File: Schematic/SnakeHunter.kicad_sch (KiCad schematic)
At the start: 17 parts, among them J1 Conn_01x04_Pin, J2 Conn_01x04_Pin, SW1 SW_Nidec_CAS-120A1, SW3 SW_DIP_x02, U2 CR2013-MI2120, U3 TSDP341xx, U4 NRF24L01_Breakout, U5 CRE1S0305S3C

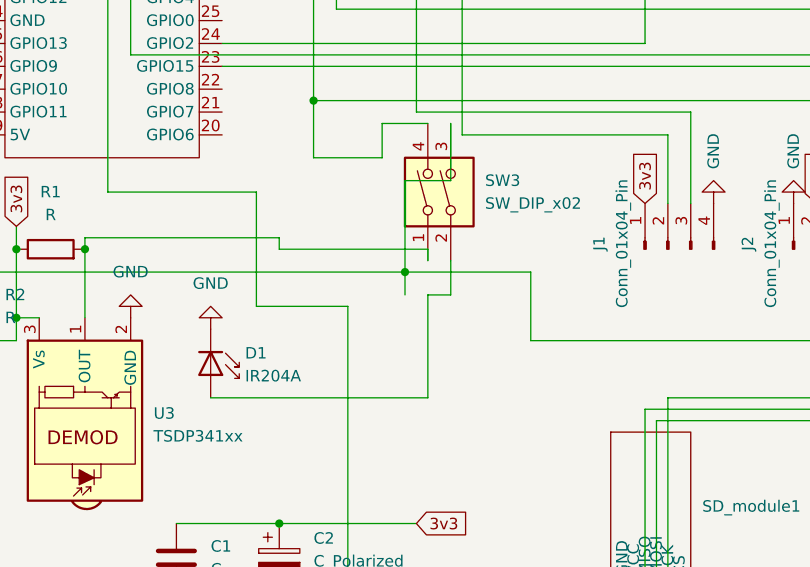
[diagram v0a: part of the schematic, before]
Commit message: Remove unused PCB because of using handwiring.
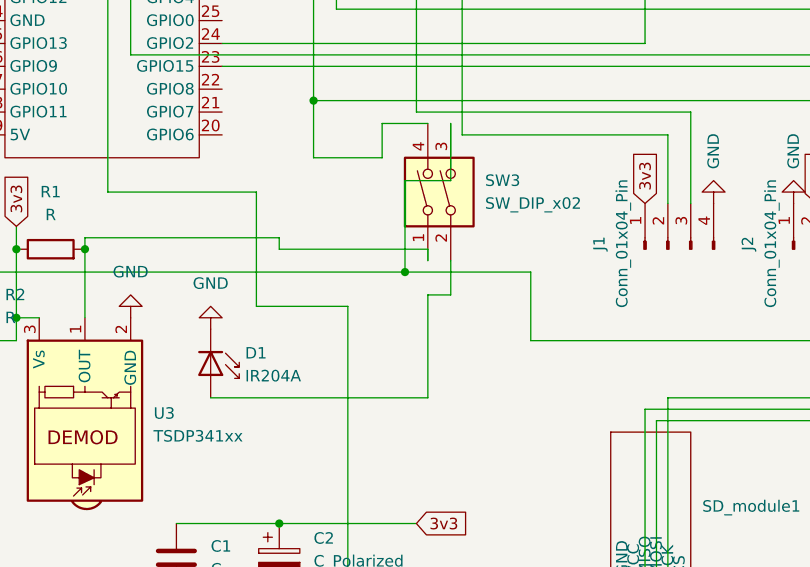
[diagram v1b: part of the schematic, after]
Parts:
- Charging_module1: footprint (none) -> my:charging chip
- J1: footprint (none) -> my:GPS
- J2: footprint (none) -> my:RFID
- R1, R2: footprint Resistor_THT:R_Array_SIP4 -> Resistor_THT:R_Axial_DIN0204_L3.6mm_D1.6mm_P5.08mm_Horizontal
- SD_module1: footprint (none) -> my:SD module
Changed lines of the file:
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@@
-	(wire
-		(pts
-			(xy 63.5 81.28) (xy 63.5 78.74)
-		)
-		(stroke
-			(width 0)
-			(type default)
-		)
-	)
 	(wire
 		(pts
@@
 			)
 		)
-		(property "Footprint" ""
+		(property "Footprint" "my:SD module"
 			(at 96.52 102.87 0)
 			(effects
@@
 			)
 		)
-		(property "Footprint" ""
+		(property "Footprint" "my:charging chip"
 			(at 156.21 121.92 0)
 			(effects
@@
 			)
 		)
-		(property "Footprint" ""
+		(property "Footprint" "my:RFID"
 			(at 109.22 76.2 0)
 			(effects
@@
 			)
 		)
-		(property "Footprint" "Resistor_THT:R_Array_SIP4"
+		(property "Footprint" "Resistor_THT:R_Axial_DIN0204_L3.6mm_D1.6mm_P5.08mm_Horizontal"
 			(at 18.288 82.55 90)
 			(effects
@@
 			)
 		)
-		(property "Footprint" ""
+		(property "Footprint" "my:GPS"
 			(at 92.71 76.2 0)
 			(effects
@@
 			)
 		)
-		(property "Footprint" "Resistor_THT:R_Array_SIP4"
+		(property "Footprint" "Resistor_THT:R_Axial_DIN0204_L3.6mm_D1.6mm_P5.08mm_Horizontal"
 			(at 24.13 77.978 90)
 			(effects

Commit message: Schematic moreee cleannn
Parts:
- J1: value Conn_01x04_Pin -> GPS module
- J2: value Conn_01x04_Pin -> RFID module
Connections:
- net GND: now also SW1.2 (B), U1.14 (GND), U2.2 (GND)
- net T-DO: now reaches U1.4 (GPI39), U2.15 (T-DO)
- net T-IRQ: now reaches U1.3 (GPI36), U2.16 (T-IRQ)
- net T-DIN: now reaches U1.7 (GPIO32), U2.17 (T-DIN)
- net T-CS: now reaches U1.8 (GPIO33), U2.18 (T-CS)
- net T-CLK: now reaches U1.9 (GPIO25), U2.19 (T-CLK)
- net CS: now reaches U1.23 (GPIO15), U2.3 (~{CS})
- net RESET: now reaches U1.2 (EN), U2.4 (RESET)
- net D/C: now reaches U1.24 (GPIO2), U2.5 (D/~{C})
- net MOSI: now reaches U1.15 (GPIO13), U2.6 (MOSI)
- net SCK: now reaches U1.12 (GPIO14), U2.7 (SCK)
- net LED: now reaches U1.33 (GPIO21), U2.8 (LED)
- net MISO: now reaches U1.13 (GPIO12), U2.9 (MISO)
- net CSN: now reaches U1.29 (GPIO5)
- net CSN: now also J2.3 (Pin_3), R2.2, SW3.3, U1.11 (GPIO27), U4.4 (~{CSN}); no longer SD_module1. (CS)
- net SCK2: now reaches SD_module1. (CS), U1.30 (GPIO18), U4.5 (SCK)
- net MISO2: now reaches SD_module1. (CS), U1.31 (GPIO19), U4.7 (MISO)
- net MOSI2: now reaches SD_module1. (CS), U1.37 (GPIO23), U4.6 (MOSI)
- net CE: now reaches J2.4 (Pin_4), SW3.4, U1.36 (GPIO22), U4.3 (CE)
- net 5v: now reaches U1.19 (5V), U5.4 (+VOUT)
- net GPIO3: now reaches J1.2 (Pin_2), U1.34 (GPIO3)
- net GPIO1: now reaches J1.3 (Pin_3), U1.35 (GPIO1)
- new net CS2: SD_module1. (CS)
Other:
- moved on the sheet: BT1, Charging_module1, D1, J2, SW1, U2, U4
